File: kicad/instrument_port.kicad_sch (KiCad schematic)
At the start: 5 parts

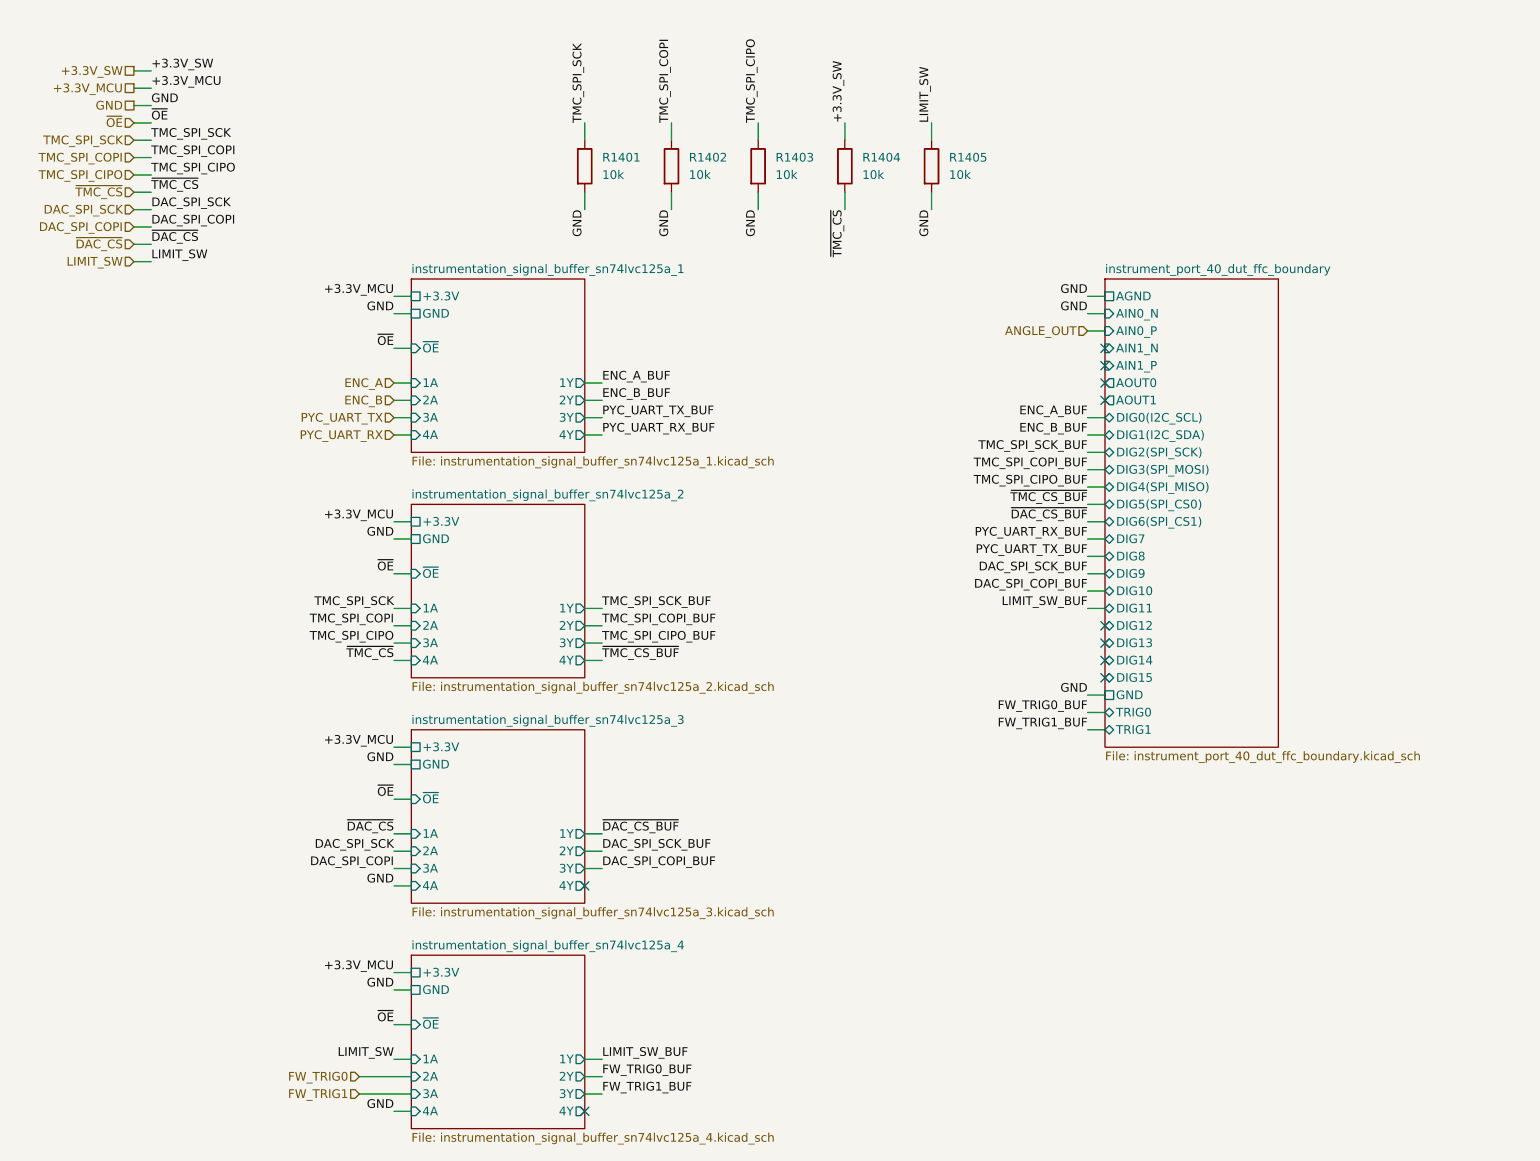
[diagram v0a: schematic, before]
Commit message: Update docs with mouse-joystick-pcb v1.0 pinout
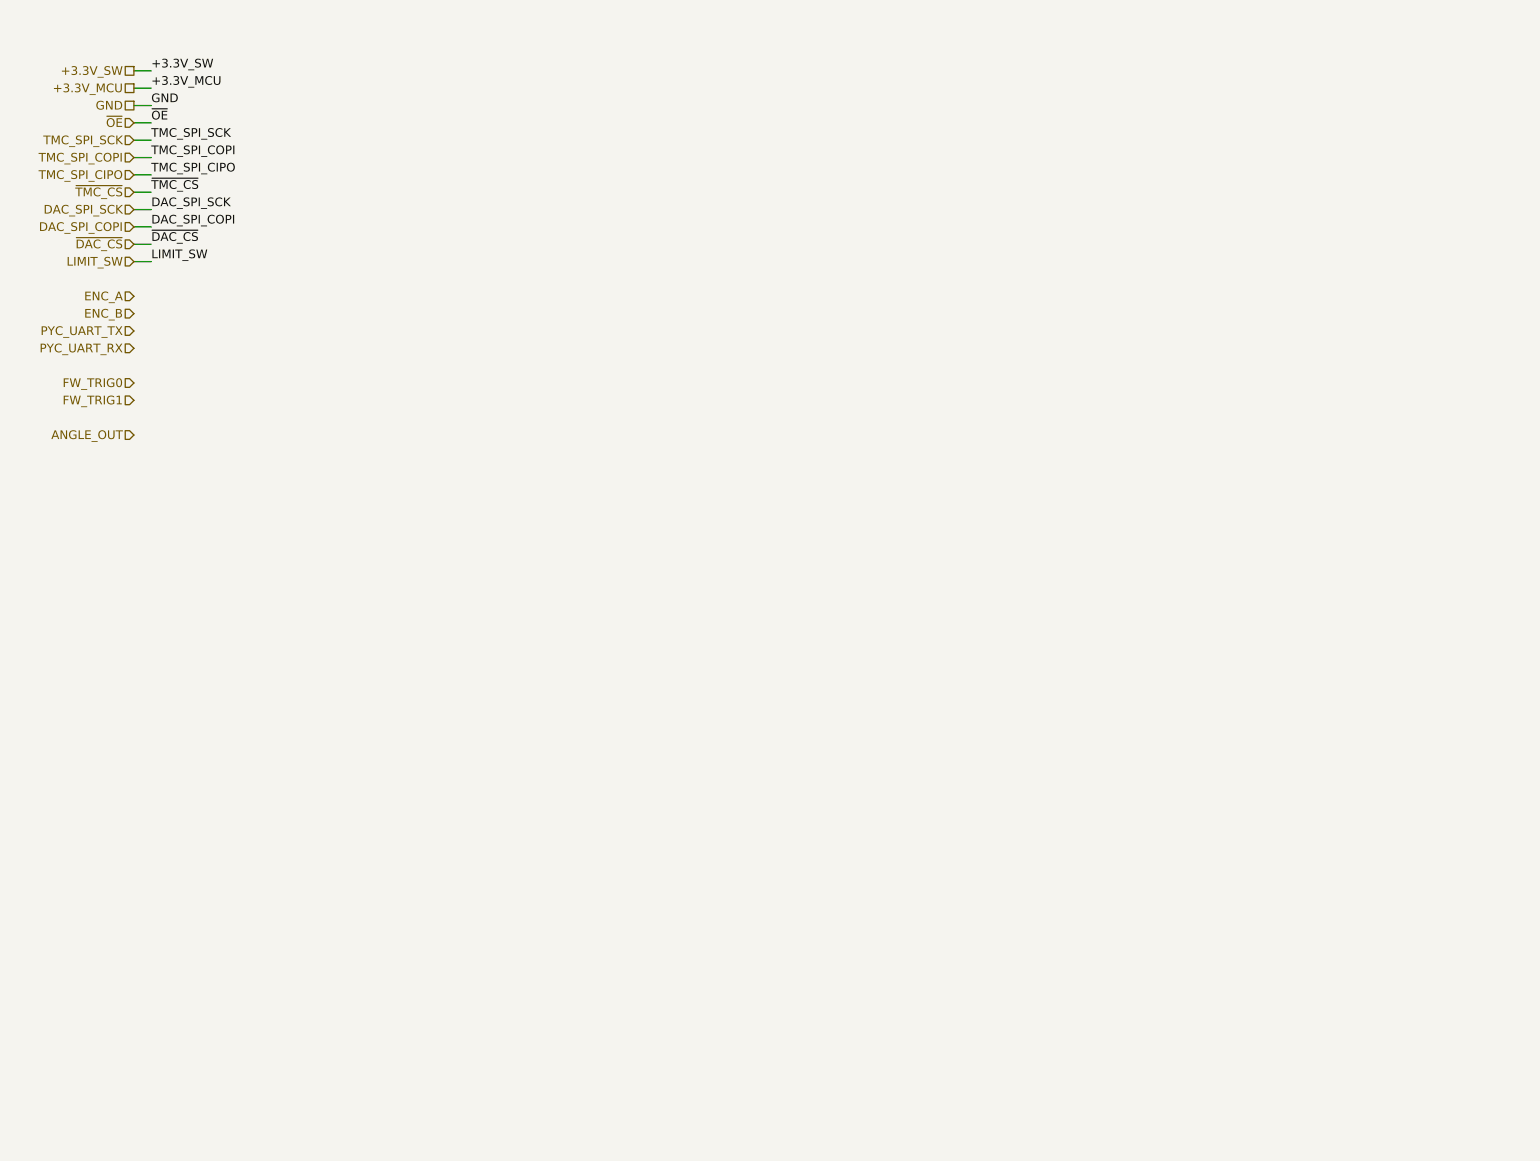
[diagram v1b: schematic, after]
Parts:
- removed R1401, R1402, R1403, R1404, R1405: 10k, Resistor_SMD:R_0402_1005Metric, symbol orb_weaver_internal:All/OW-RES-10K-0402
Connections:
- no-connect marks 10 -> 0
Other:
- removed sheet instrument_port_40_dut_ffc_boundary
- removed sheet instrumentation_signal_buffer_sn74lvc125a_1
- removed sheet instrumentation_signal_buffer_sn74lvc125a_2
- removed sheet instrumentation_signal_buffer_sn74lvc125a_3
- removed sheet instrumentation_signal_buffer_sn74lvc125a_4
- title: Orb Weaver Design Block Mining -> mouse-joystick-pcb

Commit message: Update design rules
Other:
- added sheet instrument_port_digital_50_dut_ffc_boundary_vertical (instrument_port_digital_50_dut_ffc_boundary_vertical.kicad_sch)

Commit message: Finish v1.0 schematic
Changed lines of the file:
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@@
 	(wire
 		(pts
-			(xy 127 139.7) (xy 129.54 139.7)
+			(xy 101.6 139.7) (xy 99.06 139.7)
 		)
 		(stroke
@@
 	(wire
 		(pts
-			(xy 127 137.16) (xy 129.54 137.16)
+			(xy 99.06 137.16) (xy 101.6 137.16)
 		)
 		(stroke
@@
 	)
 	(label "GND"
-		(at 129.54 139.7 0)
-		(effects
-			(font
-				(size 1.27 1.27)
-			)
-			(justify left bottom)
-		)
-	)
-	(label "GND"
 		(at 129.54 78.74 0)
 		(effects
@@
 	)
 	(label "GND"
-		(at 129.54 137.16 0)
+		(at 129.54 76.2 0)
 		(effects
 			(font
@@
 		)
 	)
-	(label "GND"
-		(at 129.54 76.2 0)
-		(effects
-			(font
-				(size 1.27 1.27)
-			)
-			(justify left bottom)
+	(hierarchical_label "PG_12V"
+		(shape input)
+		(at 99.06 139.7 180)
+		(effects
+			(font
+				(size 1.27 1.27)
+			)
+			(justify right)
 		)
 	)
@@
 		)
 	)
-	(hierarchical_label "DAQ_SDA"
+	(hierarchical_label "~{BRAKE_FAULT}"
 		(shape input)
 		(at 99.06 114.3 180)
@@
 		)
 	)
-	(hierarchical_label "TQ_SPI_COPI"
+	(hierarchical_label "TQ_CONVST_CS"
 		(shape input)
 		(at 99.06 104.14 180)
@@
 		)
 	)
-	(hierarchical_label "+3.3V_MCU"
+	(hierarchical_label "+3.3V"
 		(shape passive)
 		(at 99.06 53.34 180)
@@
 		)
 	)
+	(hierarchical_label "TMC_SPI_CIPO"
+		(shape input)
+		(at 99.06 88.9 180)
+		(effects
+			(font
+				(size 1.27 1.27)
+			)
+			(justify right)
+		)
+	)
+	(hierarchical_label "ENCA"
+		(shape input)
+		(at 99.06 132.08 180)
+		(effects
+			(font
+				(size 1.27 1.27)
+			)
+			(justify right)
+		)
+	)
+	(hierarchical_label "FW_TRIG0"
+		(shape input)
+		(at 99.06 60.96 180)
+		(effects
+			(font
+				(size 1.27 1.27)
+			)
+			(justify right)
+		)
+	)
 	(hierarchical_label "~{TMC_CS}"
 		(shape input)
-		(at 99.06 88.9 180)
-		(effects
-			(font
-				(size 1.27 1.27)
-			)
-			(justify right)
-		)
-	)
-	(hierarchical_label "ENCA"
-		(shape input)
-		(at 99.06 132.08 180)
-		(effects
-			(font
-				(size 1.27 1.27)
-			)
-			(justify right)
-		)
-	)
-	(hierarchical_label "FW_TRIG0"
-		(shape input)
-		(at 99.06 60.96 180)
+		(at 99.06 83.82 180)
 		(effects
 			(font
@@
 	)
 	(hierarchical_label "TMC_SPI_COPI"
-		(shape input)
-		(at 99.06 83.82 180)
-		(effects
-			(font
-				(size 1.27 1.27)
-			)
-			(justify right)
-		)
-	)
-	(hierarchical_label "TMC_SPI_CIPO"
 		(shape input)
 		(at 99.06 86.36 180)
@@
 		)
 	)
-	(hierarchical_label "TQ_CONVST_CS"
+	(hierarchical_label "TQ_SPI_CIPO"
 		(shape input)
 		(at 99.06 109.22 180)
@@
 		)
 	)
-	(hierarchical_label "~{BRAKE_FAULT}"
+	(hierarchical_label "PG_5V"
+		(shape input)
+		(at 99.06 137.16 180)
+		(effects
+			(font
+				(size 1.27 1.27)
+			)
+			(justify right)
+		)
+	)
+	(hierarchical_label "DAQ_SCL"
 		(shape input)
 		(at 99.06 119.38 180)
@@
 		)
 	)
-	(hierarchical_label "DAQ_SCL"
+	(hierarchical_label "DAQ_SDA"
 		(shape input)
 		(at 99.06 116.84 180)
@@
 		)
 	)
-	(hierarchical_label "TQ_SPI_CIPO"
+	(hierarchical_label "TQ_SPI_COPI"
 		(shape input)
 		(at 99.06 106.68 180)
@@
 		)
 		(pin "DIG30" input
-			(at 127 137.16 0)
-			(effects
-				(font
-					(size 1.27 1.27)
-				)
-				(justify right)
+			(at 101.6 137.16 180)
+			(effects
+				(font
+					(size 1.27 1.27)
+				)
+				(justify left)
 			)
 		)
 		(pin "DIG31" input
-			(at 127 139.7 0)
-			(effects
-				(font
-					(size 1.27 1.27)
-				)
-				(justify right)
-			)
-		)
+			(at 101.6 139.7 180)
+			(effects
+				(font
+					(size 1.27 1.27)
+				)
+				(justify left)
+			)
+		)

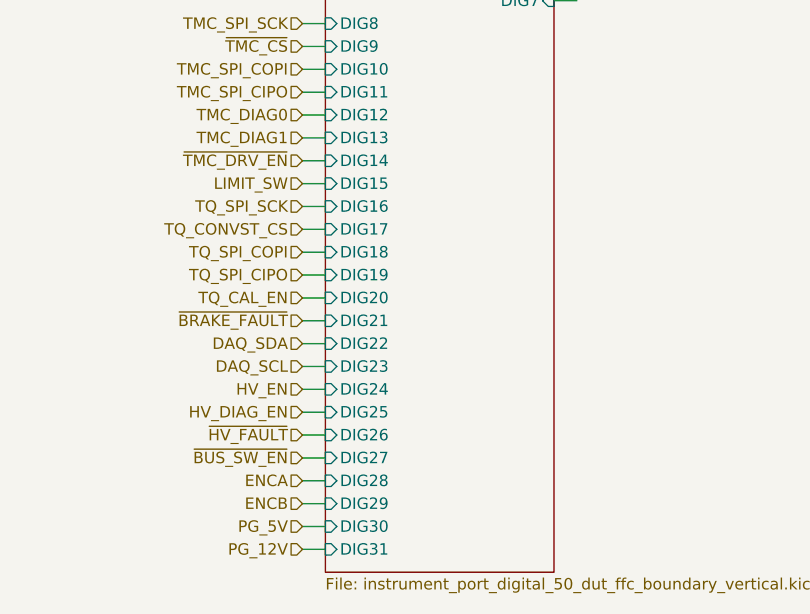
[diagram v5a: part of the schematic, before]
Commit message: Partial update of hv input block
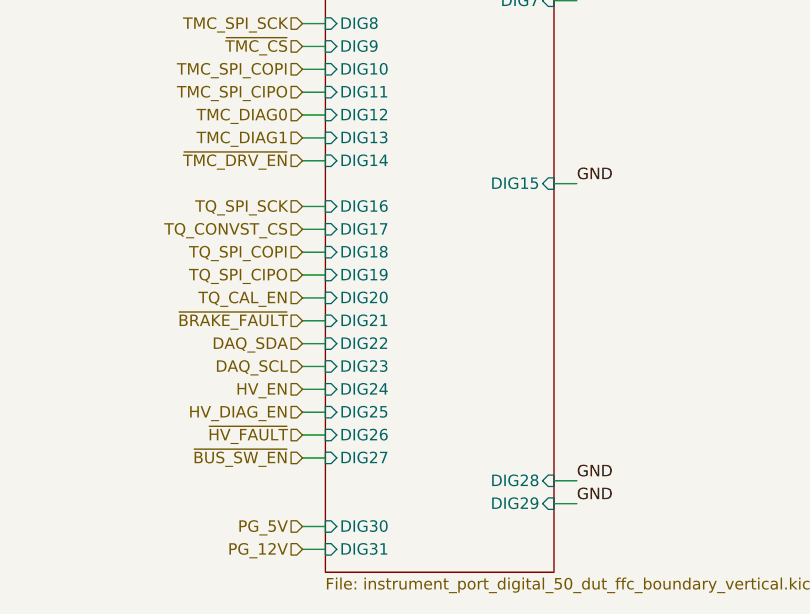
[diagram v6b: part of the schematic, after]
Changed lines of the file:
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@@
+	(wire
+		(pts
+			(xy 127 132.08) (xy 129.54 132.08)
+		)
+		(stroke
+			(width 0)
+			(type default)
+		)
+	)
 	(wire
 		(pts
@@
 	(wire
 		(pts
+			(xy 127 99.06) (xy 129.54 99.06)
+		)
+		(stroke
+			(width 0)
+			(type default)
+		)
+	)
+	(wire
+		(pts
 			(xy 127 76.2) (xy 129.54 76.2)
 		)
@@
 	(wire
 		(pts
-			(xy 99.06 99.06) (xy 101.6 99.06)
-		)
-		(stroke
-			(width 0)
-			(type default)
-		)
-	)
-	(wire
-		(pts
 			(xy 99.06 93.98) (xy 101.6 93.98)
 		)
@@
 	(wire
 		(pts
-			(xy 99.06 132.08) (xy 101.6 132.08)
-		)
-		(stroke
-			(width 0)
-			(type default)
-		)
-	)
-	(wire
-		(pts
-			(xy 99.06 134.62) (xy 101.6 134.62)
-		)
-		(stroke
-			(width 0)
-			(type default)
-		)
-	)
-	(wire
-		(pts
 			(xy 99.06 88.9) (xy 101.6 88.9)
+		)
+		(stroke
+			(width 0)
+			(type default)
+		)
+	)
+	(wire
+		(pts
+			(xy 127 134.62) (xy 129.54 134.62)
 		)
 		(stroke
@@
 	)
 	(label "GND"
+		(at 129.54 132.08 0)
+		(effects
+			(font
+				(size 1.27 1.27)
+			)
+			(justify left bottom)
+		)
+	)
+	(label "GND"
+		(at 129.54 134.62 0)
+		(effects
+			(font
+				(size 1.27 1.27)
+			)
+			(justify left bottom)
+		)
+	)
+	(label "GND"
 		(at 129.54 55.88 0)
 		(effects
@@
 	(label "GND"
 		(at 53.34 25.4 0)
+		(effects
+			(font
+				(size 1.27 1.27)
+			)
+			(justify left bottom)
+		)
+	)
+	(label "GND"
+		(at 129.54 99.06 0)
 		(effects
 			(font
@@
 		)
 	)
-	(hierarchical_label "ENCB"
-		(shape input)
-		(at 99.06 134.62 180)
-		(effects
-			(font
-				(size 1.27 1.27)
-			)
-			(justify right)
-		)
-	)
-	(hierarchical_label "LIMIT_SW"
-		(shape input)
-		(at 99.06 99.06 180)
-		(effects
-			(font
-				(size 1.27 1.27)
-			)
-			(justify right)
-		)
-	)
 	(hierarchical_label "HV_DIAG_EN"
 		(shape input)
@@
 		(shape input)
 		(at 99.06 88.9 180)
-		(effects
-			(font
-				(size 1.27 1.27)
-			)
-			(justify right)
-		)
-	)
-	(hierarchical_label "ENCA"
-		(shape input)
-		(at 99.06 132.08 180)
 		(effects
 			(font
@@
 		)
 		(pin "DIG15" input
-			(at 101.6 99.06 180)
-			(effects
-				(font
-					(size 1.27 1.27)
-				)
-				(justify left)
+			(at 127 99.06 0)
+			(effects
+				(font
+					(size 1.27 1.27)
+				)
+				(justify right)
 			)
 		)
@@
 		)
 		(pin "DIG28" input
-			(at 101.6 132.08 180)
-			(effects
-				(font
-					(size 1.27 1.27)
-				)
-				(justify left)
+			(at 127 132.08 0)
+			(effects
+				(font
+					(size 1.27 1.27)
+				)
+				(justify right)
 			)
 		)
 		(pin "DIG29" input
-			(at 101.6 134.62 180)
-			(effects
-				(font
-					(size 1.27 1.27)
-				)
-				(justify left)
-			)
-		)
+			(at 127 134.62 0)
+			(effects
+				(font
+					(size 1.27 1.27)
+				)
+				(justify right)
+			)
+		)

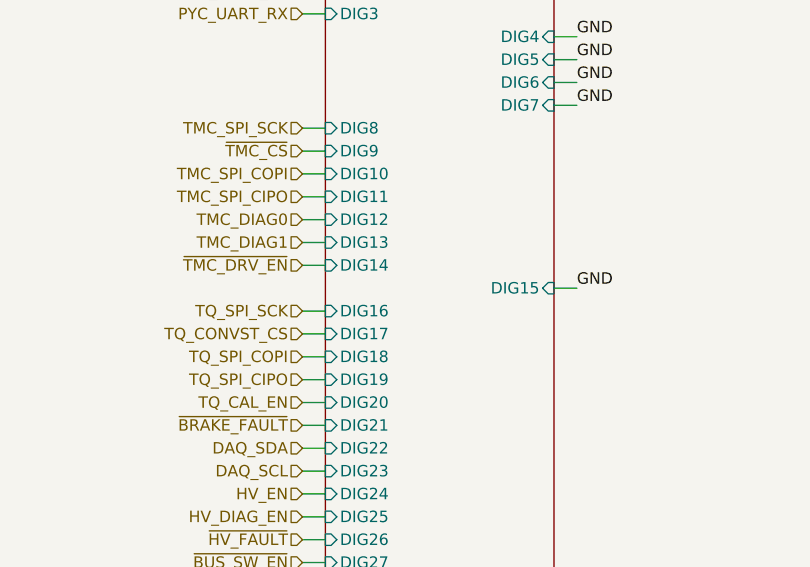
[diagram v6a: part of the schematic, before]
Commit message: Update limit switch block
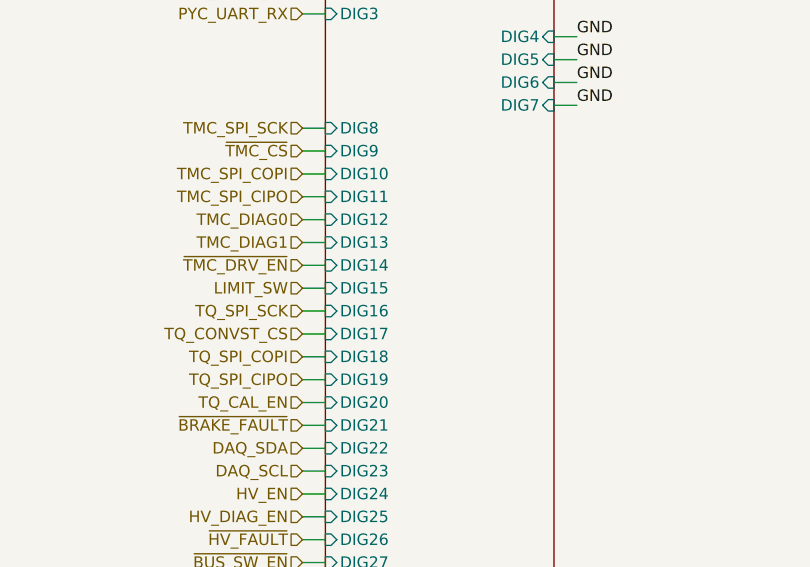
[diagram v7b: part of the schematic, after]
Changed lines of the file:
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@@
-	(wire
-		(pts
-			(xy 127 99.06) (xy 129.54 99.06)
-		)
-		(stroke
-			(width 0)
-			(type default)
-		)
-	)
 	(wire
 		(pts
@@
 		(pts
 			(xy 99.06 114.3) (xy 101.6 114.3)
+		)
+		(stroke
+			(width 0)
+			(type default)
+		)
+	)
+	(wire
+		(pts
+			(xy 99.06 99.06) (xy 101.6 99.06)
 		)
 		(stroke
@@
 	(label "GND"
 		(at 53.34 25.4 0)
-		(effects
-			(font
-				(size 1.27 1.27)
-			)
-			(justify left bottom)
-		)
-	)
-	(label "GND"
-		(at 129.54 99.06 0)
 		(effects
 			(font
@@
 		(shape input)
 		(at 99.06 129.54 180)
+		(effects
+			(font
+				(size 1.27 1.27)
+			)
+			(justify right)
+		)
+	)
+	(hierarchical_label "LIMIT_SW"
+		(shape input)
+		(at 99.06 99.06 180)
 		(effects
 			(font
@@
 		)
 		(pin "DIG15" input
-			(at 127 99.06 0)
-			(effects
-				(font
-					(size 1.27 1.27)
-				)
-				(justify right)
-			)
-		)
+			(at 101.6 99.06 180)
+			(effects
+				(font
+					(size 1.27 1.27)
+				)
+				(justify left)
+			)
+		)

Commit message: Update quadrature design block
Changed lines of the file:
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@@
 	(wire
 		(pts
-			(xy 127 132.08) (xy 129.54 132.08)
+			(xy 99.06 132.08) (xy 101.6 132.08)
 		)
 		(stroke
@@
 	(wire
 		(pts
-			(xy 127 134.62) (xy 129.54 134.62)
-		)
-		(stroke
-			(width 0)
-			(type default)
-		)
-	)
-	(wire
-		(pts
 			(xy 99.06 60.96) (xy 101.6 60.96)
 		)
@@
 		(pts
 			(xy 99.06 104.14) (xy 101.6 104.14)
+		)
+		(stroke
+			(width 0)
+			(type default)
+		)
+	)
+	(wire
+		(pts
+			(xy 99.06 134.62) (xy 101.6 134.62)
 		)
 		(stroke
@@
 	)
 	(label "GND"
-		(at 129.54 132.08 0)
-		(effects
-			(font
-				(size 1.27 1.27)
-			)
-			(justify left bottom)
-		)
-	)
-	(label "GND"
-		(at 129.54 134.62 0)
-		(effects
-			(font
-				(size 1.27 1.27)
-			)
-			(justify left bottom)
-		)
-	)
-	(label "GND"
 		(at 129.54 55.88 0)
 		(effects
@@
 		(shape input)
 		(at 99.06 121.92 180)
+		(effects
+			(font
+				(size 1.27 1.27)
+			)
+			(justify right)
+		)
+	)
+	(hierarchical_label "ENCA"
+		(shape input)
+		(at 99.06 132.08 180)
 		(effects
 			(font
@@
 		(shape input)
 		(at 99.06 91.44 180)
+		(effects
+			(font
+				(size 1.27 1.27)
+			)
+			(justify right)
+		)
+	)
+	(hierarchical_label "ENCB"
+		(shape input)
+		(at 99.06 134.62 180)
 		(effects
 			(font
@@
 		)
 		(pin "DIG28" input
-			(at 127 132.08 0)
-			(effects
-				(font
-					(size 1.27 1.27)
-				)
-				(justify right)
+			(at 101.6 132.08 180)
+			(effects
+				(font
+					(size 1.27 1.27)
+				)
+				(justify left)
 			)
 		)
 		(pin "DIG29" input
-			(at 127 134.62 0)
-			(effects
-				(font
-					(size 1.27 1.27)
-				)
-				(justify right)
-			)
-		)
+			(at 101.6 134.62 180)
+			(effects
+				(font
+					(size 1.27 1.27)
+				)
+				(justify left)
+			)
+		)
